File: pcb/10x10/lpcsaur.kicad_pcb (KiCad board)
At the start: 4 copper layers, 100 x 100 mm, 157 parts, among them IC1 74LV11, IC2 74LV10, IC3 74HCT08, IC4 74LVC07, IC5 74LVC07, IC6 LM1117-3.3, IC7 LPC1768_TQFP100, J1 X1, J10 LASER, J11 Motor X, J12 Motor Y, J13 Motor Z, J14 Motor AUX, J15 SSR, J16 SSR AUX, J17 RELAY1, J18 V-SELECT, J19 RELAY2, J2 X2, J20 V-SELECT, J21 USB_B, J22 RGB LED, J23 SERIAL, J24 5V IN, J25 12V IN, J26 24V IN, J27 AUX I/O, J28 CHILLER, J29 MICRO-SD, J3 Y1, J4 Y2, J5 Z1, J6 Z2, J7 DOOR1, J8 DOOR2, J9 E-STOP, Q1 ZXMN4A06, Q2 ZXMN4A06, Q3 BSL207SP, Q4 BSL207SP, SW1 SW_PUSH, SW2 SW_PUSH, SW3 SW_PUSH, X1 12 MHz

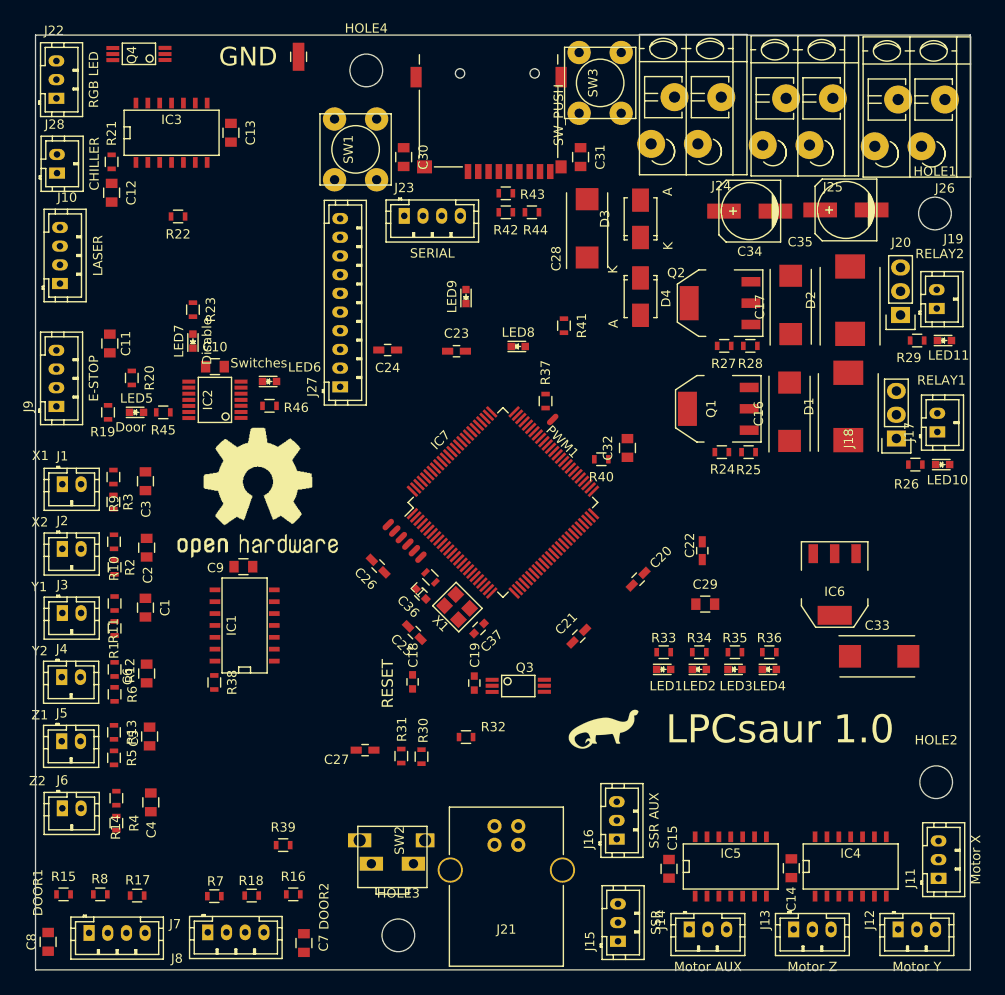
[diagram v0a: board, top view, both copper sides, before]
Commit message: Increase width of power tracks. Clean up silk screen.
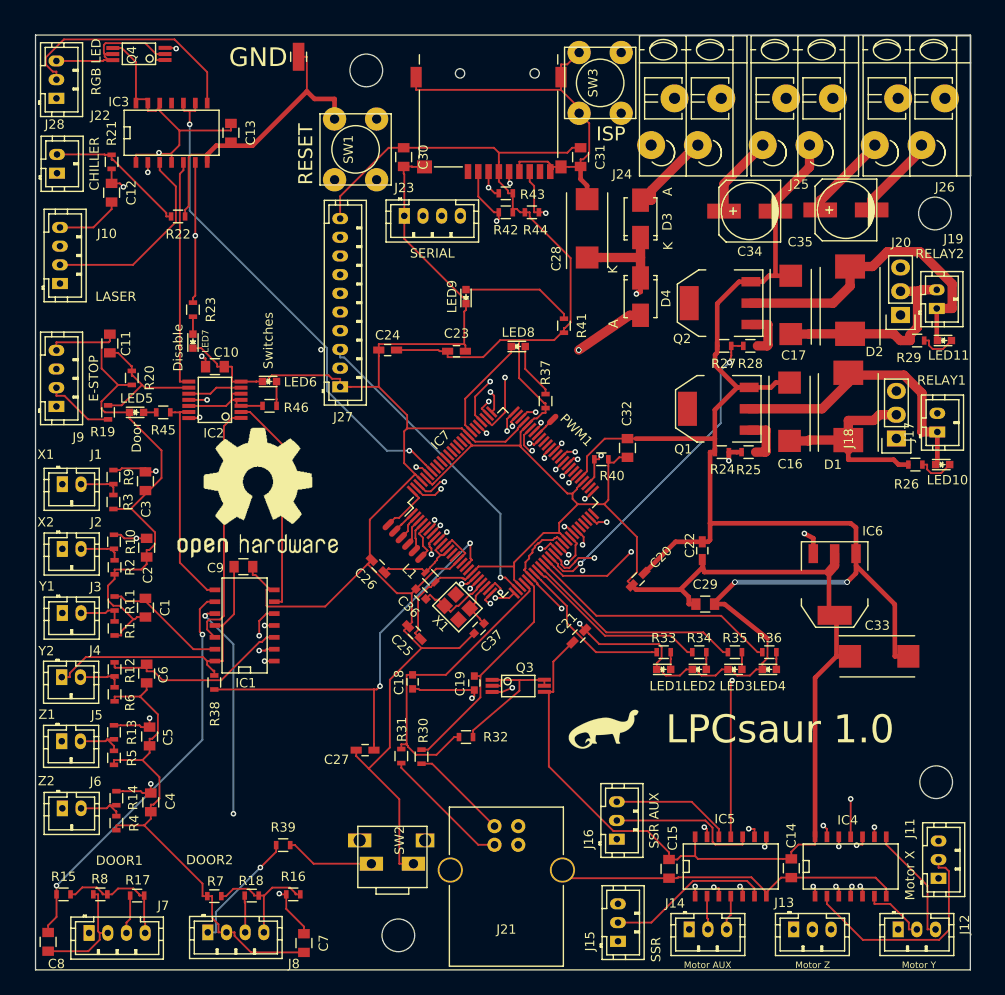
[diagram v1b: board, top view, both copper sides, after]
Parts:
- moved J26 0.13 mm to (197.3, 56.8)
- moved J24 0.13 mm to (173.4, 56.8)
- renumbered G*** to G1, G*** to G2
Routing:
- net GND: track 0.00 -> 845.6 mm, vias 0 -> 5
- net +3V3: track 0.00 -> 460.2 mm, vias 0 -> 3
- net +5V: track 0.00 -> 280.0 mm, vias 0 -> 1
- net ~RESET: track 0.00 -> 99.2 mm, vias 0 -> 2
- net Z-MAX: track 0.00 -> 73.5 mm, vias 0 -> 1
- net Z-MIN: track 0.00 -> 71.5 mm, vias 0 -> 1
- net P2.6: track 0.00 -> 69.9 mm, vias 0 -> 3
- net X-MIN: track 0.00 -> 69.2 mm, vias 0 -> 1
- net P1.31: track 0.00 -> 66.9 mm, vias 0 -> 1
- net STEP1: track 0.00 -> 66.9 mm, vias 0 -> 2
- net Y-MAX: track 0.00 -> 65.7 mm, vias 0 -> 1
- net DIR1: track 0.00 -> 65.3 mm, vias 0 -> 2
- net +12V: track 0.00 -> 65.2 mm
- net V_USB: track 0.00 -> 63.3 mm, vias 0 -> 1
- net STEP2: track 0.00 -> 61.7 mm, vias 0 -> 2
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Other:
- board text added: "ISP"
